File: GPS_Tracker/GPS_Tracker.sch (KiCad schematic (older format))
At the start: 5 parts

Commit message: added datasheets and worked on artemis module"
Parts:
- added C?: CAP, symbol pspice:CAP
- added C?: 0.1uF, symbol pspice:CAP
- added C?: 1nF, symbol pspice:CAP
- added R?: DNP, symbol Device:R
- added R?: 220K, symbol Device:R
- added R?: 100K, symbol Device:R
- added SW?: SW_Push, symbol Switch:SW_Push
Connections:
- net labels added: BOOT, DTR, RESET
- wire segments 20 -> 51
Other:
- moved on the sheet: J?

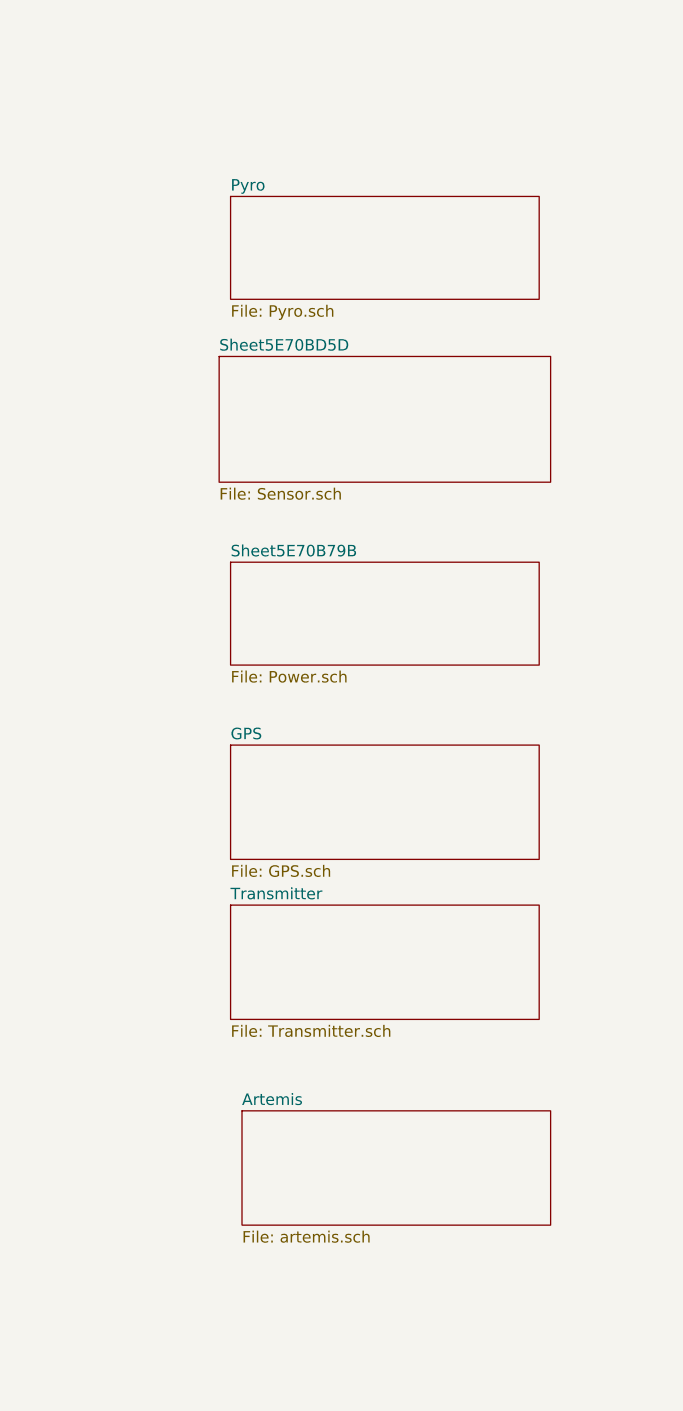
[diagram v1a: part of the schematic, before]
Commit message: added hichary labels
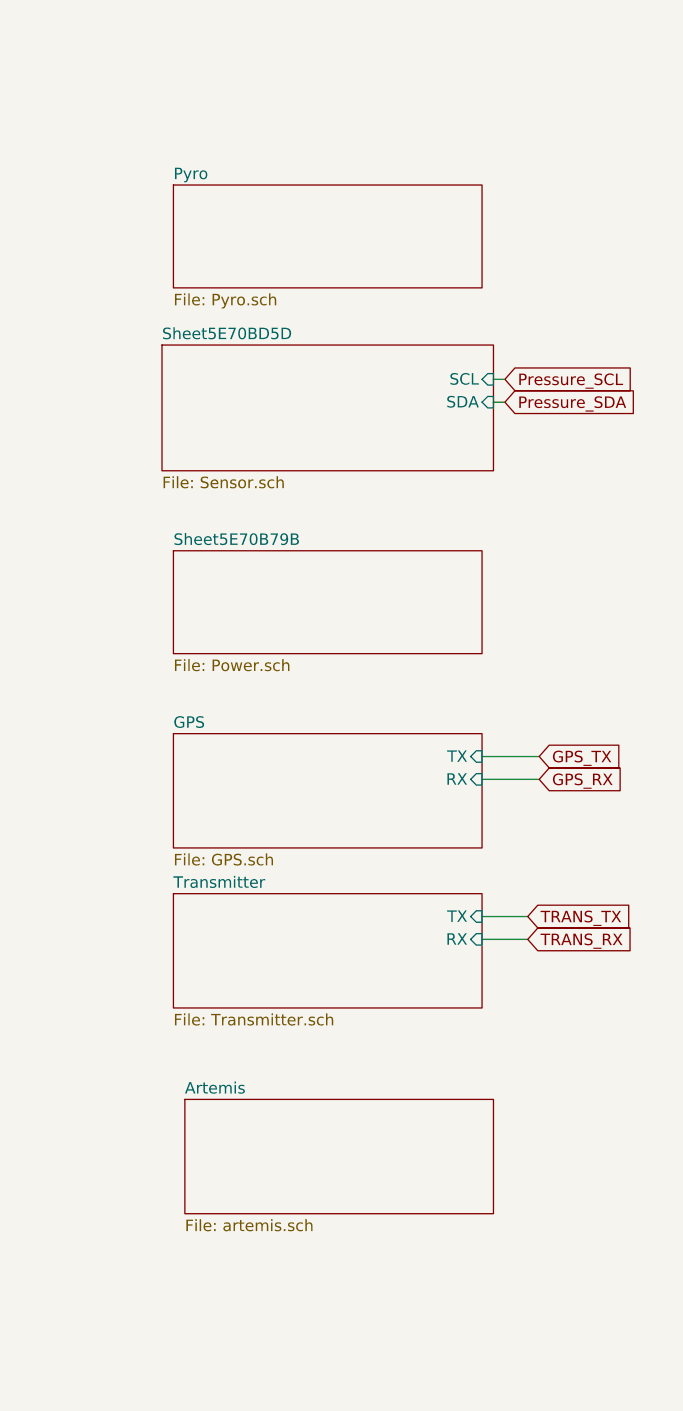
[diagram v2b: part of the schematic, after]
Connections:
- net labels added: GPS_RX, GPS_TX, Pressure_SCL, Pressure_SDA, TRANS_RX, TRANS_TX
- wire segments 51 -> 57
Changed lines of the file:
@@
 $EndComp
 $Sheet
-S 9200 5400 1350 500
+S 8950 5350 1350 500
 U 5E6FE21E
 F0 "Artemis" 50
@@
 $EndSheet
 $Sheet
-S 9150 4500 1350 500
+S 8900 4450 1350 500
 U 5E70A48E
 F0 "Transmitter" 50
 F1 "Transmitter.sch" 50
-$EndSheet
-$Sheet
-S 9150 3800 1350 500
+F2 "TX" I R 10250 4550 50
+F3 "RX" I R 10250 4650 50
+$EndSheet
+$Sheet
+S 8900 3750 1350 500
 U 5E70A878
 F0 "GPS" 50
 F1 "GPS.sch" 50
-$EndSheet
-$Sheet
-S 9150 3000 1350 450
+F2 "TX" I R 10250 3850 50
+F3 "RX" I R 10250 3950 50
+$EndSheet
+$Sheet
+S 8900 2950 1350 450
 U 5E70B79C
 F0 "Sheet5E70B79B" 50
@@
 $EndSheet
 $Sheet
-S 9100 2100 1450 550
+S 8850 2050 1450 550
 U 5E70BD5E
 F0 "Sheet5E70BD5D" 50
 F1 "Sensor.sch" 50
+F2 "SCL" I R 10300 2200 50
+F3 "SDA" I R 10300 2300 50
 $EndSheet
 $Comp
@@
 	2650 3000 2650 2800
 $Sheet
-S 9150 1400 1350 450
+S 8900 1350 1350 450
 U 5E714987
 F0 "Pyro" 50
@@
 Wire Wire Line
 	6200 5950 6200 6050
+Text GLabel 10500 3850 2    50   Input ~ 0
+GPS_TX
+Text GLabel 10500 3950 2    50   Input ~ 0
+GPS_RX
+Wire Wire Line
+	10250 3850 10500 3850
+Wire Wire Line
+	10250 3950 10500 3950
+Text GLabel 10450 4550 2    50   Input ~ 0
+TRANS_TX
+Text GLabel 10450 4650 2    50   Input ~ 0
+TRANS_RX
+Wire Wire Line
+	10250 4550 10450 4550
+Wire Wire Line
+	10250 4650 10450 4650
+Text GLabel 10350 2200 2    50   Input ~ 0
+Pressure_SCL
+Text GLabel 10350 2300 2    50   Input ~ 0
+Pressure_SDA
+Wire Wire Line
+	10300 2200 10350 2200
+Wire Wire Line
+	10300 2300 10350 2300
 $EndSCHEMATC

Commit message: added usb
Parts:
- removed J?: Conn_ARM_JTAG_SWD_10, symbol Connector:Conn_ARM_JTAG_SWD_10
- added C?: 10nF, symbol pspice:CAP
- added C?: 0.1uF, symbol pspice:CAP
- added D? (x2): LED, symbol Device:LED
- added J?: USB_C_Receptacle, symbol Connector:USB_C_Receptacle
- added R? (x2): 1K, symbol Device:R
- added U?: CH340E, MSOP10, symbol Sparkfun~Artemis:CH340E
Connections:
- net labels added: RTS, RX1, TXD
- net labels removed: SWDCK, SWDIO
- wire segments 57 -> 77
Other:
- moved on the sheet: C?, R?, SW?

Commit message: updated labels;
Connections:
- net labels added: RX0, RXI, TX0, TXO
- net labels removed: RX1, TXD
- wire segments 77 -> 79
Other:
- moved on the sheet: C?, D?, J?, R?, SW?, Y?
